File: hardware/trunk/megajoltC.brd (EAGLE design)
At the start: 79.9 x 63 mm, 117 parts, among them IC1 IC_FT230X-SSOP-16, IC2 MCP1826, IC3 MCP1826, J3 JUMPER_CLOSEDTHICK, U1 MCP1700, U11 TLV274, U12 PESDXS4UD, U18 MCP2551SO8, U4 ZXMS6004FF, U8 FAN8303, X1 MINI_USB_SHIELD

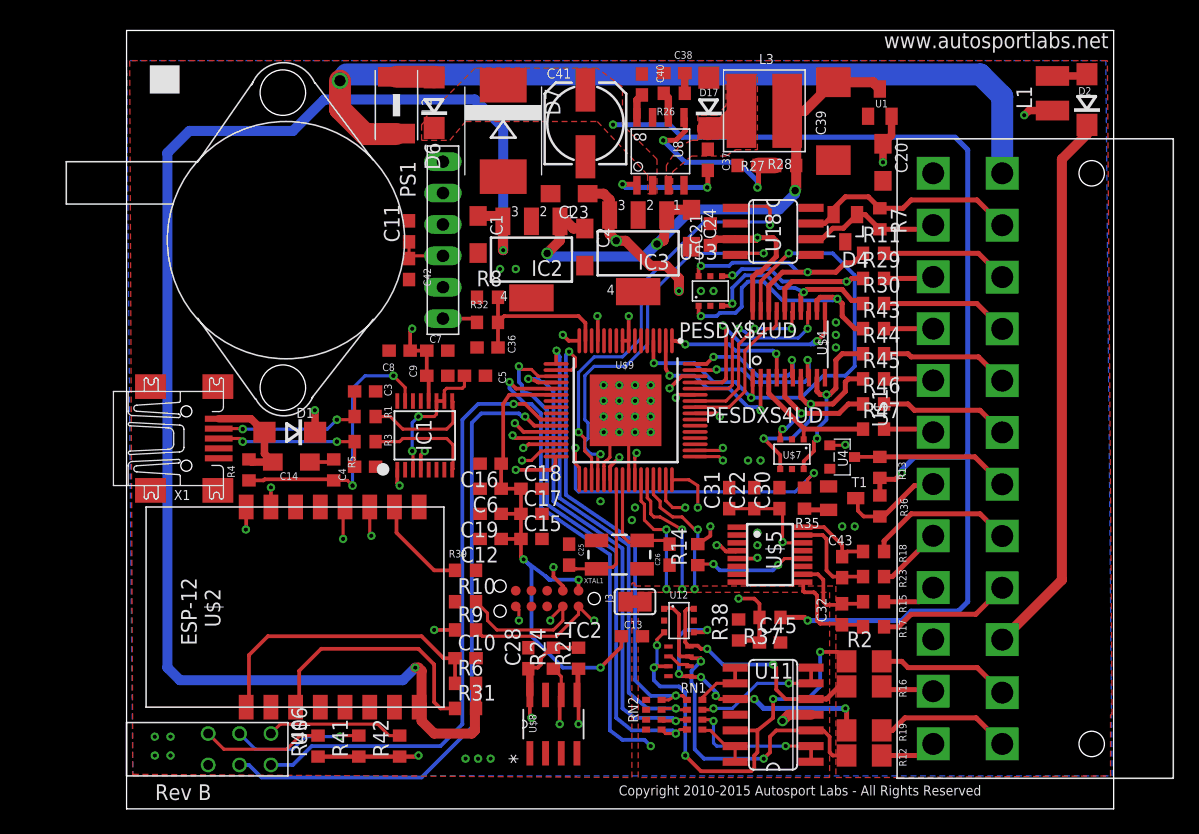
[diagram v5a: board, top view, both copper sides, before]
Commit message: Change label size on board.  Add additional gnd stitching
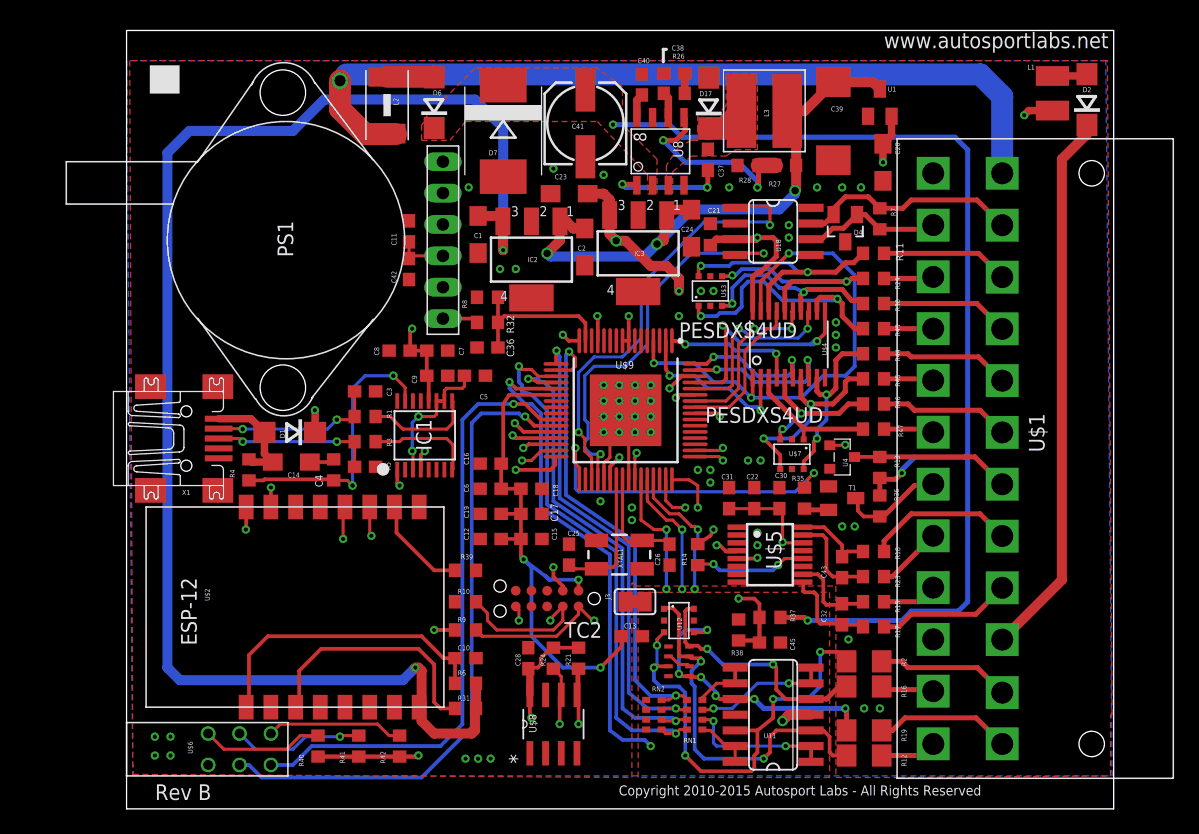
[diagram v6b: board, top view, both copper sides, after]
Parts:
- moved L2 0.76 mm to (21.1, 56.9)
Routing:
- net N$15: track 3.07 -> 3.83 mm
- net RAW_+12V: track 68.5 -> 69.2 mm
- net GND: vias 37 -> 53
